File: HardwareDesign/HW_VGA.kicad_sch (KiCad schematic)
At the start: 4 parts, among them J401 Conn_01x06, U1 25.175 MHz, U301 GAL22V10

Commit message: starting over on VRAM readout hardware
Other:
- removed sheet ReadAddr
- removed sheet ReadVRAM
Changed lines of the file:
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@@
-	)
-	(sheet
-		(at 191.77 115.57)
-		(size 27.94 45.72)
-		(fields_autoplaced yes)
-		(stroke
-			(width 0.1524)
-			(type solid)
-		)
-		(fill
-			(color 0 0 0 0.0000)
-		)
-		(property "Sheetname" "ReadVRAM"
-			(at 191.77 114.8584 0)
-			(effects
-				(font
-					(size 1.27 1.27)
-				)
-				(justify left bottom)
-			)
-		)
-		(property "Sheetfile" "ReadVRAM.kicad_sch"
-			(at 191.77 161.8746 0)
-			(effects
-				(font
-					(size 1.27 1.27)
-				)
-				(justify left top)
-			)
-		)
-		(instances
-			(project "HW_VGA"
-				(path "/c4bd4b39-993a-4195-805f-b4de6fa4aea5"
-					(page "7")
-				)
-			)
-		)
-	)
-	(sheet
-		(at 152.4 120.65)
-		(size 26.67 39.37)
-		(fields_autoplaced yes)
-		(stroke
-			(width 0.1524)
-			(type solid)
-		)
-		(fill
-			(color 0 0 0 0.0000)
-		)
-		(property "Sheetname" "ReadAddr"
-			(at 152.4 119.9384 0)
-			(effects
-				(font
-					(size 1.27 1.27)
-				)
-				(justify left bottom)
-			)
-		)
-		(property "Sheetfile" "ReadAddr.kicad_sch"
-			(at 152.4 160.6046 0)
-			(effects
-				(font
-					(size 1.27 1.27)
-				)
-				(justify left top)
-			)
-		)
-		(pin "CLK" input
-			(at 152.4 124.46 180)
-			(effects
-				(font
-					(size 1.27 1.27)
-				)
-				(justify left)
-			)
-		)
-		(pin "-CLR" input
-			(at 152.4 127 180)
-			(effects
-				(font
-					(size 1.27 1.27)
-				)
-				(justify left)
-			)
-		)
-		(pin "CountEn" input
-			(at 152.4 129.54 180)
-			(effects
-				(font
-					(size 1.27 1.27)
-				)
-				(justify left)
-			)
-		)
-		(pin "RA7" output
-			(at 179.07 142.24 0)
-			(effects
-				(font
-					(size 1.27 1.27)
-				)
-				(justify right)
-			)
-		)
-		(pin "RA6" output
-			(at 179.07 139.7 0)
-			(effects
-				(font
-					(size 1.27 1.27)
-				)
-				(justify right)
-			)
-		)
-		(pin "RA5" output
-			(at 179.07 137.16 0)
-			(effects
-				(font
-					(size 1.27 1.27)
-				)
-				(justify right)
-			)
-		)
-		(pin "RA0" output
-			(at 179.07 124.46 0)
-			(effects
-				(font
-					(size 1.27 1.27)
-				)
-				(justify right)
-			)
-		)
-		(pin "RA1" output
-			(at 179.07 127 0)
-			(effects
-				(font
-					(size 1.27 1.27)
-				)
-				(justify right)
-			)
-		)
-		(pin "RA2" output
-			(at 179.07 129.54 0)
-			(effects
-				(font
-					(size 1.27 1.27)
-				)
-				(justify right)
-			)
-		)
-		(pin "RA3" output
-			(at 179.07 132.08 0)
-			(effects
-				(font
-					(size 1.27 1.27)
-				)
-				(justify right)
-			)
-		)
-		(pin "RA4" output
-			(at 179.07 134.62 0)
-			(effects
-				(font
-					(size 1.27 1.27)
-				)
-				(justify right)
-			)
-		)
-		(pin "RA8" output
-			(at 179.07 144.78 0)
-			(effects
-				(font
-					(size 1.27 1.27)
-				)
-				(justify right)
-			)
-		)
-		(pin "RA9" output
-			(at 179.07 147.32 0)
-			(effects
-				(font
-					(size 1.27 1.27)
-				)
-				(justify right)
-			)
-		)
-		(pin "RA10" output
-			(at 179.07 149.86 0)
-			(effects
-				(font
-					(size 1.27 1.27)
-				)
-				(justify right)
-			)
-		)
-		(pin "RA11" output
-			(at 179.07 152.4 0)
-			(effects
-				(font
-					(size 1.27 1.27)
-				)
-				(justify right)
-			)
-		)
-		(pin "RA12" output
-			(at 179.07 154.94 0)
-			(effects
-				(font
-					(size 1.27 1.27)
-				)
-				(justify right)
-			)
-		)
-		(instances
-			(project "HW_VGA"
-				(path "/c4bd4b39-993a-4195-805f-b4de6fa4aea5"
-					(page "5")
-				)
-			)
-		)
 	)
 	(sheet

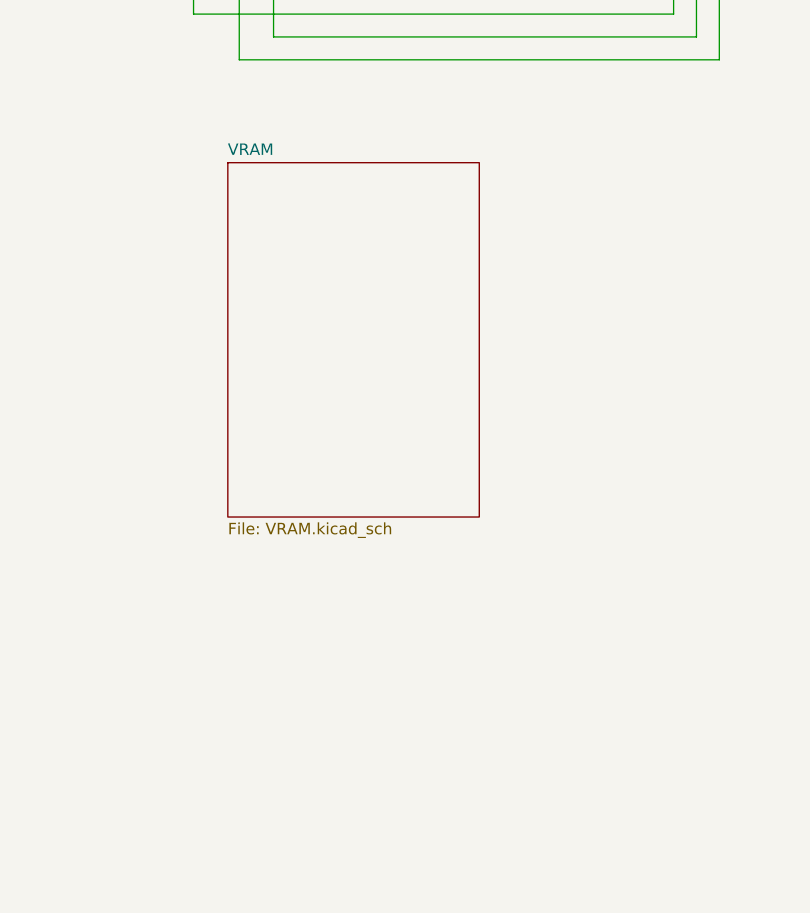
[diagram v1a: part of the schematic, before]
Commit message: import hierarchical pins for VRAM sheet
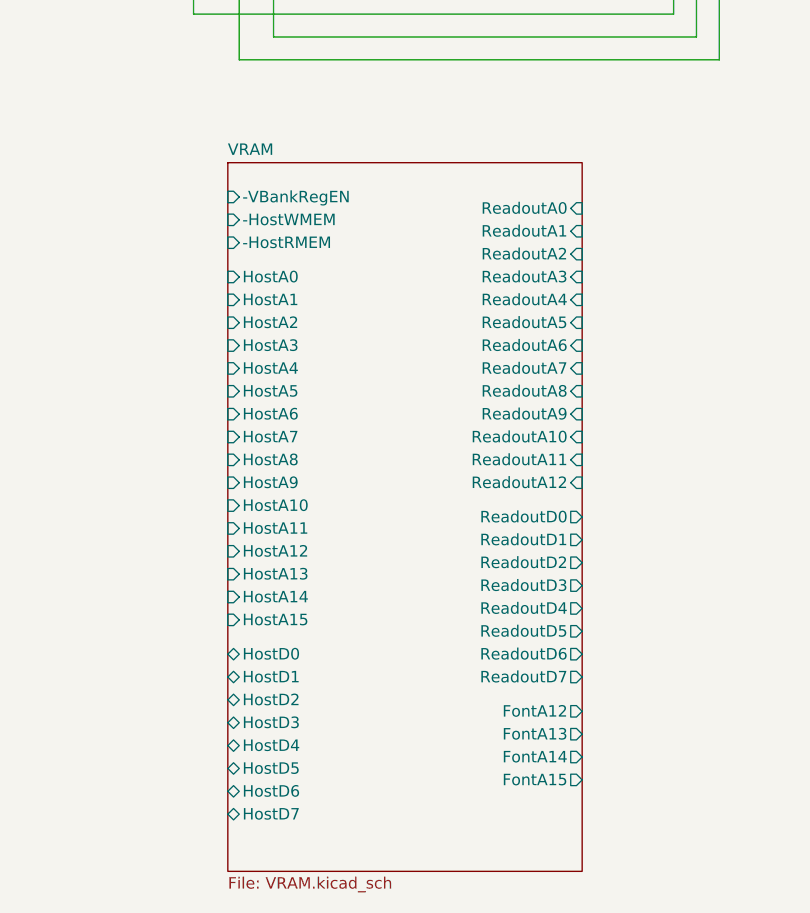
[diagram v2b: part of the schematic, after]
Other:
- sheet VRAM ports: added -HostRMEM, -HostWMEM, -VBankRegEN, FontA12, FontA13, FontA14, FontA15, HostA0, HostA1, HostA10, HostA11, HostA12, HostA13, HostA14, HostA15, HostA2, HostA3, HostA4, HostA5, HostA6, HostA7, HostA8, HostA9, HostD0, HostD1, HostD2, HostD3, HostD4, HostD5, HostD6, HostD7, ReadoutA0, ReadoutA1, ReadoutA10, ReadoutA11, ReadoutA12, ReadoutA2, ReadoutA3, ReadoutA4, ReadoutA5, ReadoutA6, ReadoutA7, ReadoutA8, ReadoutA9, ReadoutD0, ReadoutD1, ReadoutD2, ReadoutD3, ReadoutD4, ReadoutD5, ReadoutD6, ReadoutD7; removed none
